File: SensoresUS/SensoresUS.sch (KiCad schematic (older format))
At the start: 7 parts

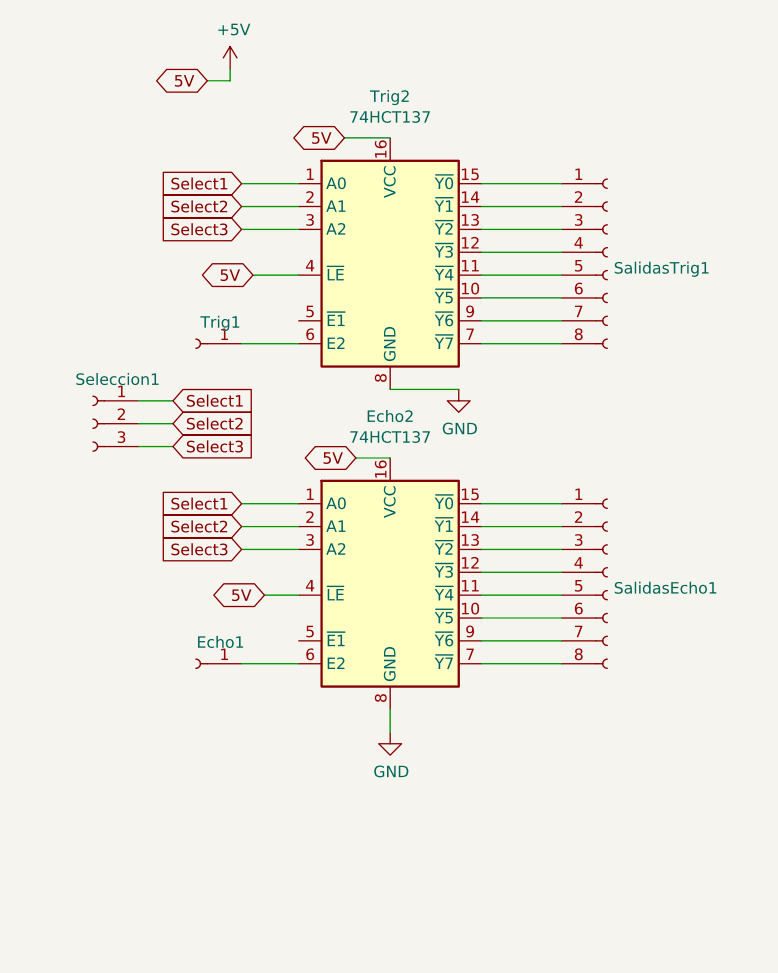
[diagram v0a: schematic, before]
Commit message: Placa SUS
Cambio de integrados
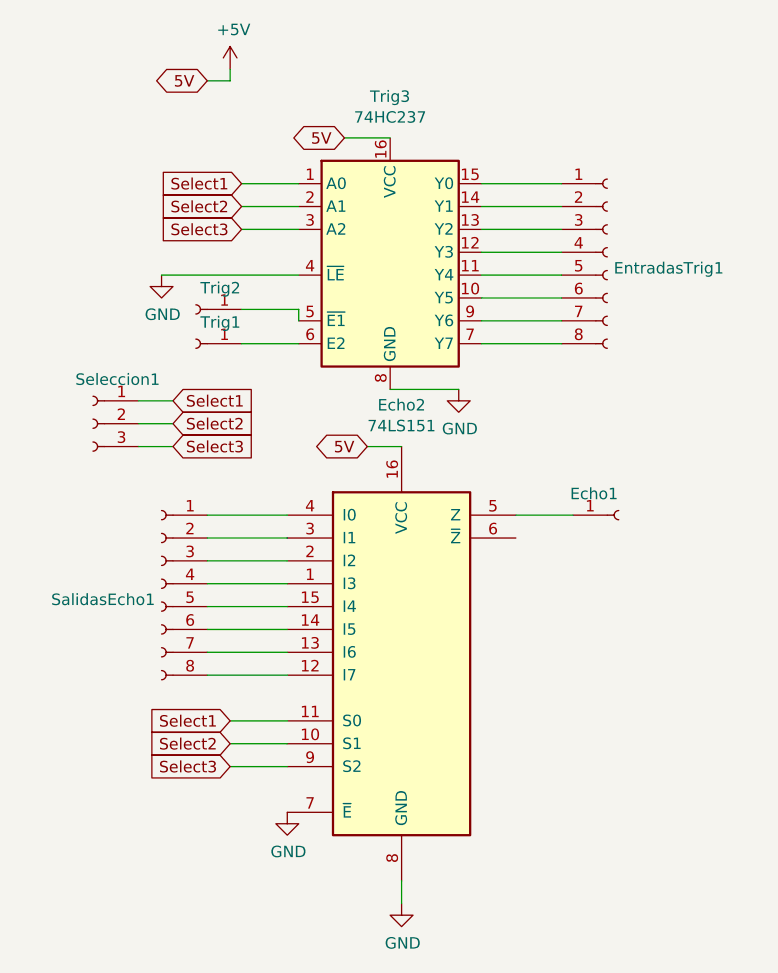
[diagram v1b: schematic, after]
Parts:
- removed Echo2, Trig2: 74HCT137, Package_DIP:DIP-16_W7.62mm_LongPads, symbol 74xx:74HCT137
- added Echo2: 74LS151, Package_DIP:DIP-16_W7.62mm_LongPads, symbol 74xx:74LS151
- added Trig2: Conn_01x01_Female, symbol Connector:Conn_01x01_Female
- added Trig3: 74HC237, Package_DIP:DIP-16_W7.62mm_LongPads, symbol 74xx:74HC237
- Echo1: footprint Connector_Molex:Molex_KK-254_AE-6410-05A_1x05_P2.54mm_Vertical -> Connector_Molex:Molex_KK-254_AE-6410-06A_1x06_P2.54mm_Vertical
- Trig1: footprint (none) -> Connector_Molex:Molex_KK-254_AE-6410-02A_1x02_P2.54mm_Vertical
- renumbered SalidasTrig1 to EntradasTrig1
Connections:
- net +5V: now also Echo2.16 (VCC), Trig3.16 (VCC)
- net GND: now also Echo2.7 (~E), Echo2.8 (GND), Trig3.4 (~LE), Trig3.8 (GND)
- net Select1: now also Echo2.11 (S0), Trig3.1 (A0)
- net Select2: now also Echo2.10 (S1), Trig3.2 (A1)
- net Select3: now also Echo2.9 (S2), Trig3.3 (A2)
- net at SalidasEcho1.6 (Pin_6): now also Echo2.14 (I5)
- net at SalidasEcho1.5 (Pin_5): now also Echo2.15 (I4)
- net at SalidasEcho1.4 (Pin_4): now also Echo2.1 (I3)
- net at SalidasEcho1.3 (Pin_3): now also Echo2.2 (I2)
- net at SalidasEcho1.2 (Pin_2): now also Echo2.3 (I1)
- net at SalidasEcho1.1 (Pin_1): now also Echo2.4 (I0)
- net at Echo1.1 (Pin_1): now also Echo2.5 (Z)
- net at SalidasEcho1.8 (Pin_8): now also Echo2.12 (I7)
- net at SalidasEcho1.7 (Pin_7): now also Echo2.13 (I6)
- net at EntradasTrig1.6 (Pin_6): now also Trig3.10 (Y5)
- net at EntradasTrig1.5 (Pin_5): now also Trig3.11 (Y4)
- net at EntradasTrig1.4 (Pin_4): now also Trig3.12 (Y3)
- net at EntradasTrig1.3 (Pin_3): now also Trig3.13 (Y2)
- net at EntradasTrig1.2 (Pin_2): now also Trig3.14 (Y1)
- net at EntradasTrig1.1 (Pin_1): now also Trig3.15 (Y0)
- net at Trig1.1 (Pin_1): now also Trig3.6 (E2)
- net at EntradasTrig1.8 (Pin_8): now also Trig3.7 (Y7)
- net at EntradasTrig1.7 (Pin_7): now also Trig3.9 (Y6)
- new net: Trig2.1 (Pin_1), Trig3.5 (~E1)
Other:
- moved on the sheet: Echo1, SalidasEcho1
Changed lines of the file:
@@
 $EndDescr
-$Comp
-L 74xx:74HCT137 Echo2
-U 1 1 5EDE6D7B
-P 5700 4750
-F 0 "Echo2" H 5700 5531 50  0000 C CNN
-F 1 "74HCT137" H 5700 5440 50  0000 C CNN
-F 2 "Package_DIP:DIP-16_W7.62mm_LongPads" H 5700 4750 50  0001 C CNN
-F 3 "http://www.ti.com/lit/ds/symlink/cd74hc237.pdf" H 5700 4750 50  0001 C CNN
-	1    5700 4750
-	1    0    0    -1
-$EndComp
 $Comp
 L Connector:Conn_01x08_Female SalidasEcho1
 U 1 1 5EDF2DE8
-P 6650 4650
-F 0 "SalidasEcho1" H 6678 4580 50  0000 L CNN
-F 1 "Conn_01x08_Female" H 6678 4535 50  0001 L CNN
-F 2 "Connector_Molex:Molex_KK-254_AE-6410-08A_1x08_P2.54mm_Vertical" H 6650 4650 50  0001 C CNN
-F 3 "~" H 6650 4650 50  0001 C CNN
-	1    6650 4650
-	1    0    0    -1
-$EndComp
-Wire Wire Line
-	6100 4350 6450 4350
-Wire Wire Line
-	6100 4450 6450 4450
-Wire Wire Line
-	6100 4550 6450 4550
-Wire Wire Line
-	6100 4650 6450 4650
-Wire Wire Line
-	6100 4750 6450 4750
-Wire Wire Line
-	6100 4850 6450 4850
-Wire Wire Line
-	6100 4950 6450 4950
-Wire Wire Line
-	6100 5050 6450 5050
+P 4700 4700
+F 0 "SalidasEcho1" H 4728 4630 50  0000 L CNN
+F 1 "Conn_01x08_Female" H 4728 4585 50  0001 L CNN
+F 2 "Connector_Molex:Molex_KK-254_AE-6410-08A_1x08_P2.54mm_Vertical" H 4700 4700 50  0001 C CNN
+F 3 "~" H 4700 4700 50  0001 C CNN
+	1    4700 4700
+	-1   0    0    -1
+$EndComp
+Wire Wire Line
+	5250 4400 4900 4400
+Wire Wire Line
+	5250 4500 4900 4500
+Wire Wire Line
+	5250 4600 4900 4600
+Wire Wire Line
+	5250 4700 4900 4700
+Wire Wire Line
+	5250 4800 4900 4800
+Wire Wire Line
+	5250 4900 4900 4900
+Wire Wire Line
+	5250 5000 4900 5000
+Wire Wire Line
+	5250 5100 4900 5100
 $Comp
 L Connector:Conn_01x03_Female Seleccion1
@@
 Wire Wire Line
 	4600 4100 4750 4100
-Text GLabel 5050 4350 0    50   Input ~ 0
+Text GLabel 5000 5300 0    50   Input ~ 0
 Select1
-Text GLabel 5050 4450 0    50   Input ~ 0
+Text GLabel 5000 5400 0    50   Input ~ 0
 Select2
-Text GLabel 5050 4550 0    50   Input ~ 0
+Text GLabel 5000 5500 0    50   Input ~ 0
 Select3
 Wire Wire Line
-	5050 4350 5300 4350
-Wire Wire Line
-	5050 4450 5300 4450
-Wire Wire Line
-	5050 4550 5300 4550
-$Comp
-L Connector:Conn_01x08_Female SalidasTrig1
+	5000 5300 5250 5300
+Wire Wire Line
+	5000 5400 5250 5400
+Wire Wire Line
+	5000 5500 5250 5500
+$Comp
+L Connector:Conn_01x08_Female EntradasTrig1
 U 1 1 5EE0315F
 P 6650 3250
-F 0 "SalidasTrig1" H 6678 3180 50  0000 L CNN
+F 0 "EntradasTrig1" H 6678 3180 50  0000 L CNN
 F 1 "Conn_01x08_Female" H 6542 3644 50  0001 C CNN
 F 2 "Connector_Molex:Molex_KK-254_AE-6410-08A_1x08_P2.54mm_Vertical" H 6650 3250 50  0001 C CNN
@@
 F 0 "Trig1" H 4742 3743 50  0000 C CNN
 F 1 "Conn_01x01_Female" H 4742 3744 50  0001 C CNN
-F 2 "" H 4850 3650 50  0001 C CNN
+F 2 "Connector_Molex:Molex_KK-254_AE-6410-02A_1x02_P2.54mm_Vertical" H 4850 3650 50  0001 C CNN
 F 3 "~" H 4850 3650 50  0001 C CNN
 	1    4850 3650
@@
 L Connector:Conn_01x01_Female Echo1
 U 1 1 5EE08B55
-P 4850 5050
-F 0 "Echo1" H 4742 5143 50  0000 C CNN
-F 1 "Conn_01x01_Female" H 4742 5144 50  0001 C CNN
-F 2 "Connector_Molex:Molex_KK-254_AE-6410-05A_1x05_P2.54mm_Vertical" H 4850 5050 50  0001 C CNN
-F 3 "~" H 4850 5050 50  0001 C CNN
-	1    4850 5050
-	-1   0    0    -1
-$EndComp
-Wire Wire Line
-	5050 5050 5300 5050
+P 6700 4400
+F 0 "Echo1" H 6592 4493 50  0000 C CNN
+F 1 "Conn_01x01_Female" H 6592 4494 50  0001 C CNN
+F 2 "Connector_Molex:Molex_KK-254_AE-6410-06A_1x06_P2.54mm_Vertical" H 6700 4400 50  0001 C CNN
+F 3 "~" H 6700 4400 50  0001 C CNN
+	1    6700 4400
+	1    0    0    -1
+$EndComp
+Wire Wire Line
+	6500 4400 6250 4400
 Wire Wire Line
 	5050 3650 5300 3650
@@
 	1    0    0    -1
 $EndComp
-$Comp
-L 74xx:74HCT137 Trig2
-U 1 1 5EE03155
-P 5700 3350
-F 0 "Trig2" H 5700 4131 50  0000 C CNN
-F 1 "74HCT137" H 5700 4040 50  0000 C CNN
-F 2 "Package_DIP:DIP-16_W7.62mm_LongPads" H 5700 3350 50  0001 C CNN
-F 3 "http://www.ti.com/lit/ds/symlink/cd74hc237.pdf" H 5700 3350 50  0001 C CNN
-	1    5700 3350
-	1    0    0    -1
-$EndComp
 Text GLabel 4900 2500 0    50   BiDi ~ 0
 5V
 Text GLabel 5500 2750 0    50   BiDi ~ 0
 5V
-Text GLabel 5550 4150 0    50   BiDi ~ 0
-5V
-Wire Wire Line
-	5550 4150 5700 4150
 Wire Wire Line
 	5500 2750 5700 2750
@@
 L power:GND #PWR0102
 U 1 1 5EE138C4
-P 5700 5350
-F 0 "#PWR0102" H 5700 5100 50  0001 C CNN
-F 1 "GND" H 5705 5177 50  0000 C CNN
-F 2 "" H 5700 5350 50  0001 C CNN
-F 3 "" H 5700 5350 50  0001 C CNN
-	1    5700 5350
+P 5750 6100
+F 0 "#PWR0102" H 5750 5850 50  0001 C CNN
+F 1 "GND" H 5755 5927 50  0000 C CNN
+F 2 "" H 5750 6100 50  0001 C CNN
+F 3 "" H 5750 6100 50  0001 C CNN
+	1    5750 6100
 	1    0    0    -1
 $EndComp
@@
 	5700 3850 6000 3850
 Wire Wire Line
-	5700 5250 5700 5350
-Text GLabel 5100 3350 0    50   BiDi ~ 0
+	5750 6000 5750 6100
+Text GLabel 5600 4100 0    50   BiDi ~ 0
 5V
-Text GLabel 5150 4750 0    50   BiDi ~ 0
-5V
-Wire Wire Line
-	5150 4750 5300 4750
-Wire Wire Line
-	5100 3350 5300 3350
+Wire Wire Line
+	5600 4100 5750 4100
+$Comp
+L 74xx:74HC237 Trig3
+U 1 1 5EDE9FF8
+P 5700 3350
+F 0 "Trig3" H 5700 4131 50  0000 C CNN
+F 1 "74HC237" H 5700 4040 50  0000 C CNN
+F 2 "Package_DIP:DIP-16_W7.62mm_LongPads" H 5700 3350 50  0001 C CNN
+F 3 "http://www.ti.com/lit/ds/symlink/cd74hc237.pdf" H 5700 3350 50  0001 C CNN
+	1    5700 3350
+	1    0    0    -1
+$EndComp
+$Comp
+L power:GND #PWR0104
+U 1 1 5EDEB9F0
+P 4700 3350
+F 0 "#PWR0104" H 4700 3100 50  0001 C CNN
+F 1 "GND" H 4705 3177 50  0000 C CNN
+F 2 "" H 4700 3350 50  0001 C CNN
+F 3 "" H 4700 3350 50  0001 C CNN
+	1    4700 3350
+	1    0    0    -1
+$EndComp
+Wire Wire Line
+	5300 3350 4700 3350
+$Comp
+L Connector:Conn_01x01_Female Trig2
+U 1 1 5EDED08B
+P 4850 3500
+F 0 "Trig2" H 4742 3593 50  0000 C CNN
+F 1 "Conn_01x01_Female" H 4742 3594 50  0001 C CNN
+F 2 "" H 4850 3500 50  0001 C CNN
+F 3 "~" H 4850 3500 50  0001 C CNN
+	1    4850 3500
+	-1   0    0    -1
+$EndComp
+Wire Wire Line
+	5050 3500 5300 3500
+Wire Wire Line
+	5300 3500 5300 3550
+$Comp
+L 74xx:74LS151 Echo2
+U 1 1 5EDEF353
+P 5750 5000
+F 0 "Echo2" H 5750 6081 50  0000 C CNN
+F 1 "74LS151" H 5750 5990 50  0000 C CNN
+F 2 "Package_DIP:DIP-16_W7.62mm_LongPads" H 5750 5000 50  0001 C CNN
+F 3 "http://www.ti.com/lit/gpn/sn74LS151" H 5750 5000 50  0001 C CNN
+	1    5750 5000
+	1    0    0    -1
+$EndComp
+$Comp
+L power:GND #PWR0105
+U 1 1 5EE064BB
+P 5250 5700
+F 0 "#PWR0105" H 5250 5450 50  0001 C CNN
+F 1 "GND" H 5255 5527 50  0000 C CNN
+F 2 "" H 5250 5700 50  0001 C CNN
+F 3 "" H 5250 5700 50  0001 C CNN
+	1    5250 5700
+	1    0    0    -1
+$EndComp
 $EndSCHEMATC
